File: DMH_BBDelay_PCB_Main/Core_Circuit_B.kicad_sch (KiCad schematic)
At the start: 68 parts, among them Q8 J113, SW1 SW_DPDT_x2, SW2 SW_DPDT_x2, SW4 SW_SPDT, U5 TL074, U6 TL074, U7 V3205, U8 CD4046, U9 40106

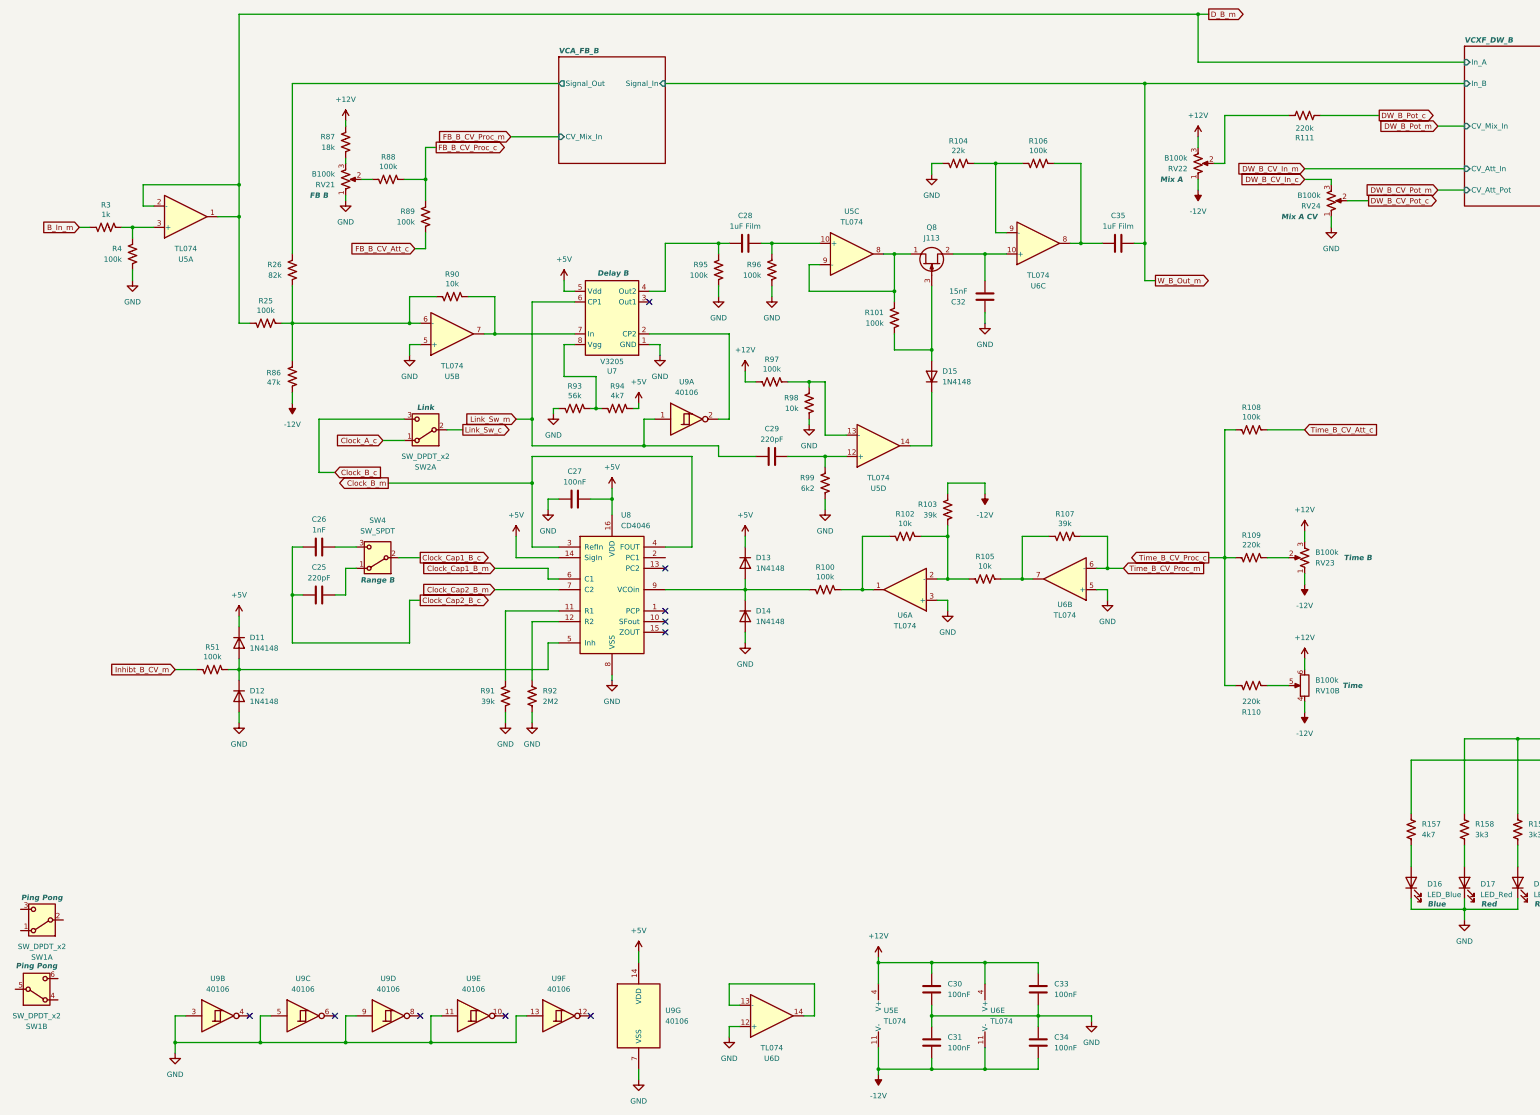
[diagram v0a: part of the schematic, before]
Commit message: Schematic in progress
Added AC coupling to inputs
Buffered wet outputs
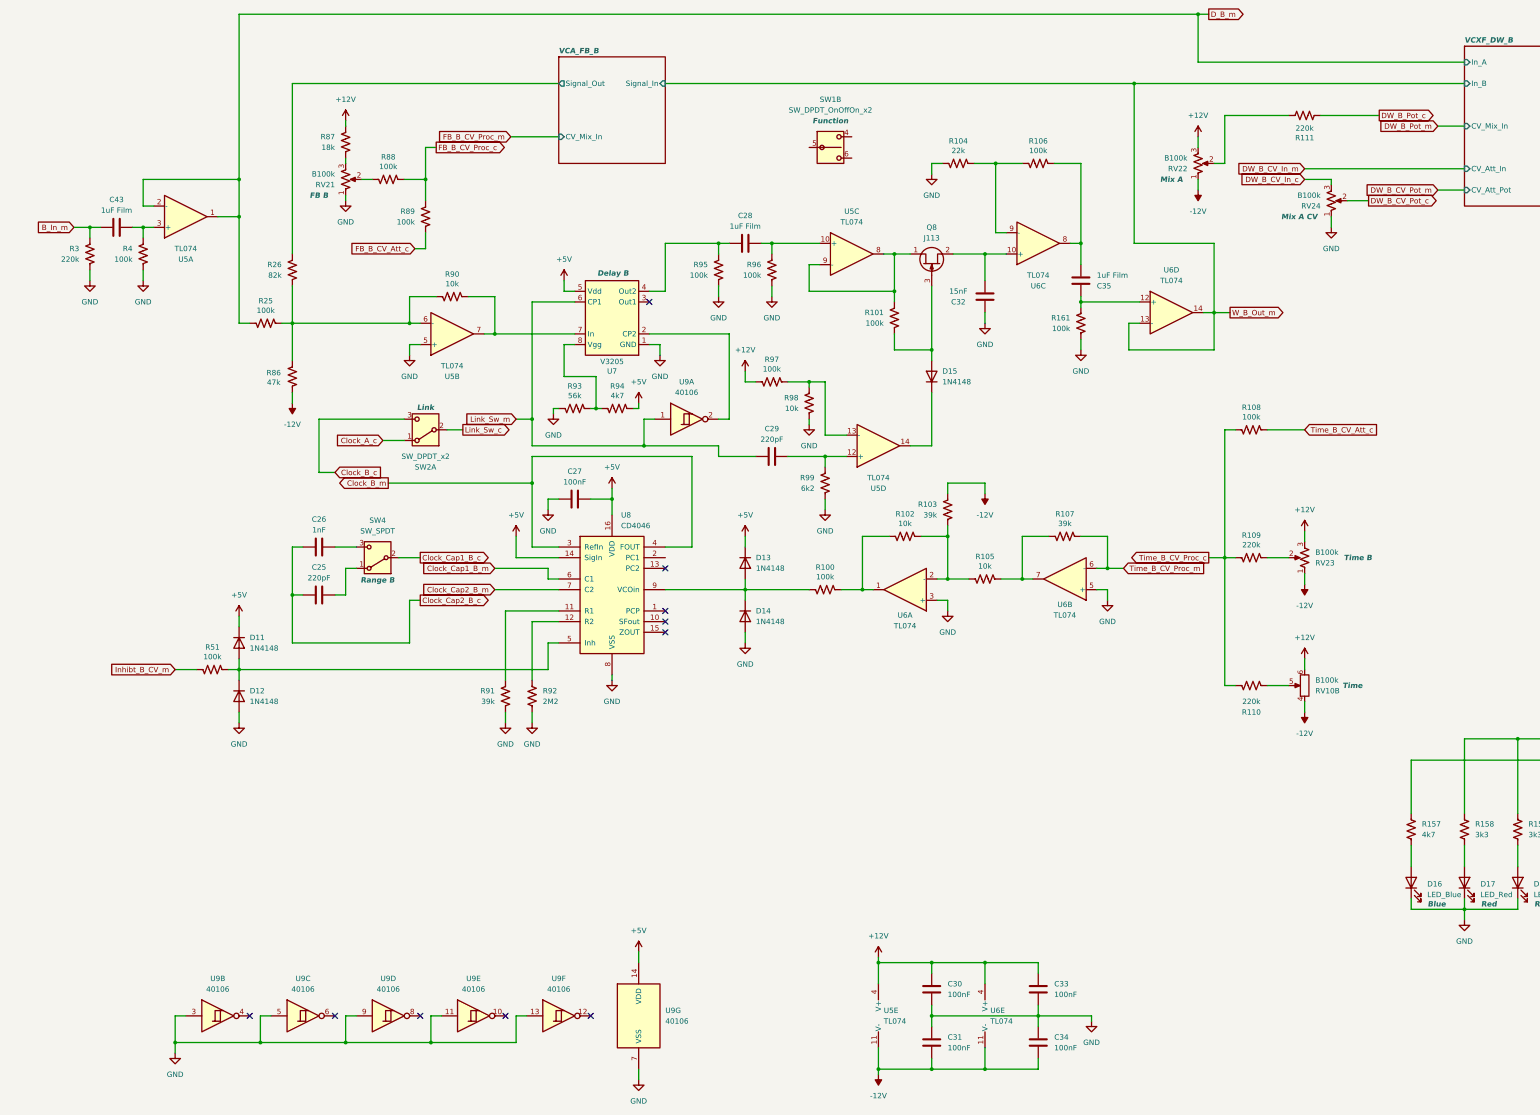
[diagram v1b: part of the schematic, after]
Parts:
- removed SW1: SW_DPDT_x2, symbol Switch:SW_DPDT_x2
- added C43: 1uF Film, Capacitor_THT:C_Disc_D7.5mm_W5.0mm_P5.00mm, symbol Device:C
- added R161: 100k, Resistor_THT:R_Axial_DIN0207_L6.3mm_D2.5mm_P7.62mm_Horizontal, symbol Device:R_US
- added SW1: SW_DPDT_OnOffOn_x2, SynthStuff:Toggle_Switch_2_Poles_TE, symbol SynthStuff:SW_DPDT_OnOffOn_x2
- C28, C35: footprint Capacitor_THT:C_Disc_D7.5mm_W4.4mm_P5.00mm -> Capacitor_THT:C_Disc_D7.5mm_W5.0mm_P5.00mm
- R3: value 1k -> 220k
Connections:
- net B_In_m: now also R3.2, C43.1; no longer R3.1
- net GND: now also R3.1, R161.1; no longer U6.12 (+)
- net W_B_Out_m: now also U6.13 (-), U6.14; no longer C35.2
- net at R4.2, U5.3 (+): now also C43.2; no longer R3.2
- net at R106.2, U6.8: now also C35.2; no longer C35.1
- new net: C35.1, R161.2, U6.12 (+)
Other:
- moved on the sheet: C35, R4, U6D

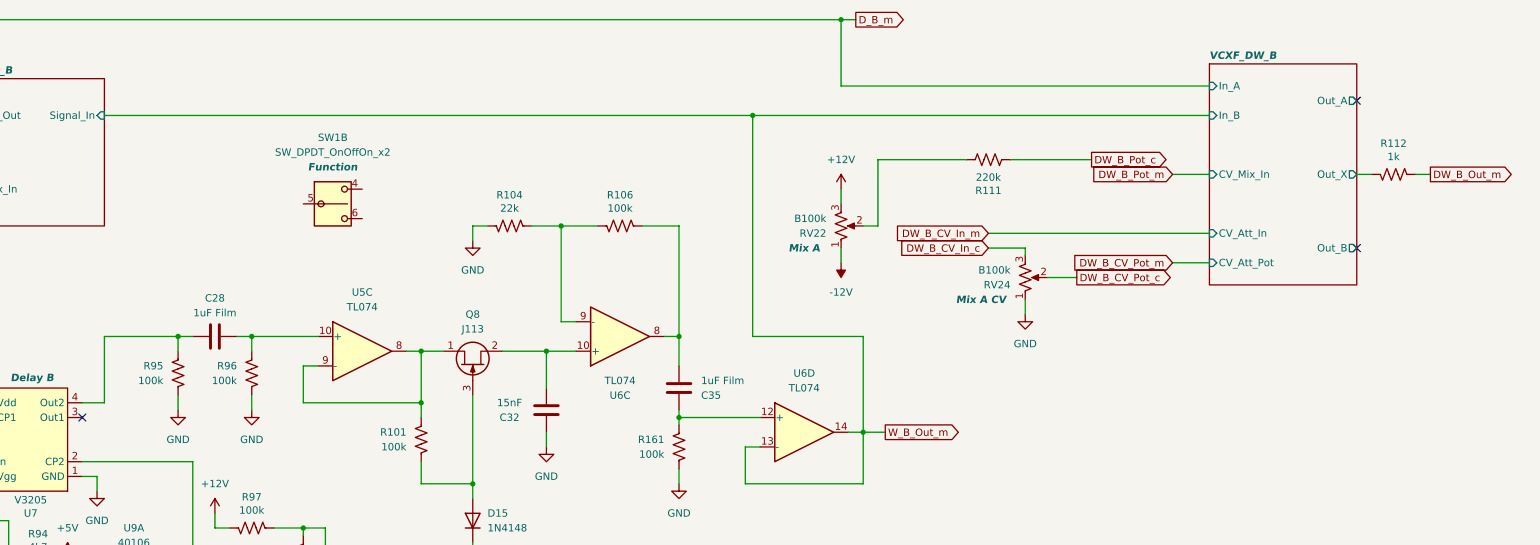
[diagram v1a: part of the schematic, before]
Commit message: Implemented Ping Pong funtion
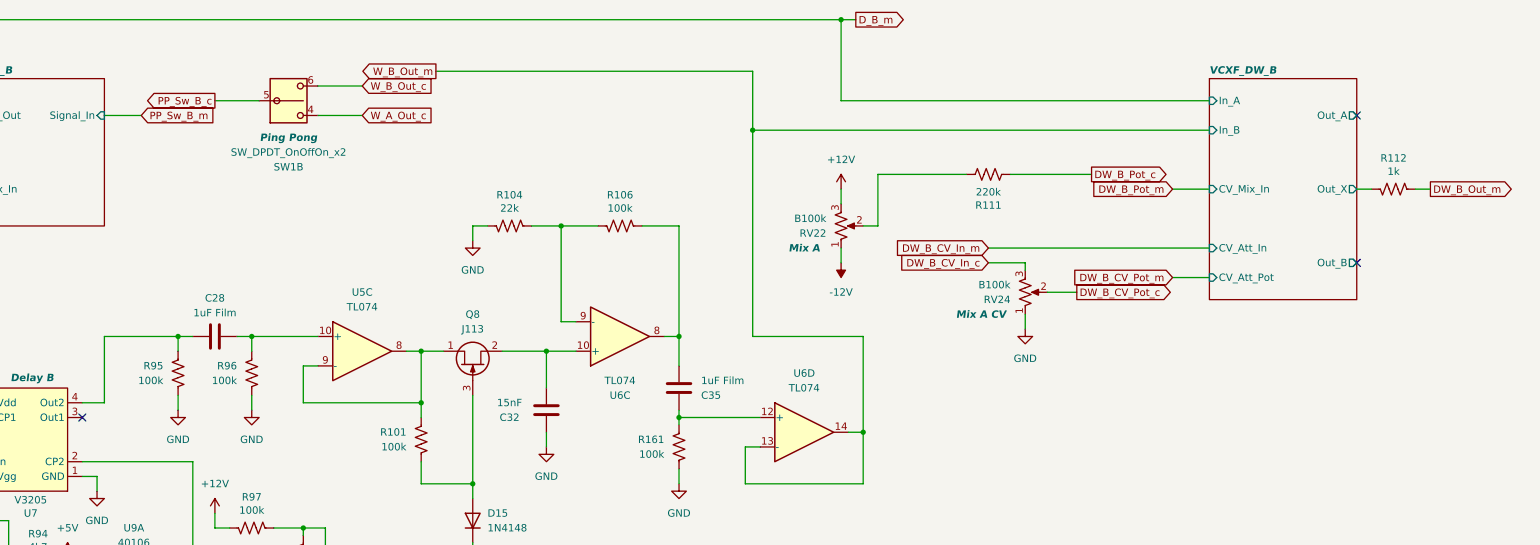
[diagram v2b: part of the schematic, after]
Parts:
- SW1: Function Function -> Ping Pong
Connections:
- net W_A_Out_c: now reaches SW1.4 (A)
- net PP_Sw_B_c: now reaches SW1.5 (B)
- net W_B_Out_c: now reaches SW1.6 (C)
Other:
- moved on the sheet: R111, R112, RV24, SW1B

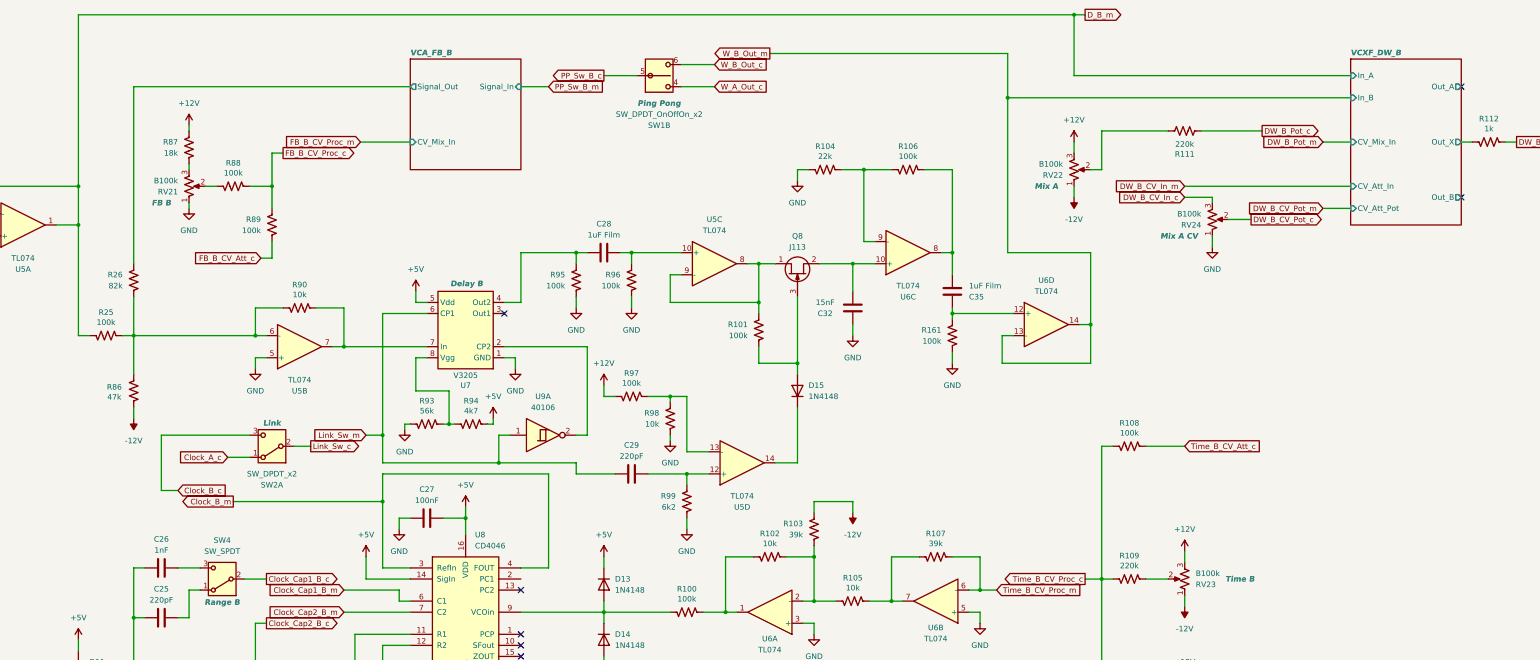
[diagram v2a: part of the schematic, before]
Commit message: Implemented tone control
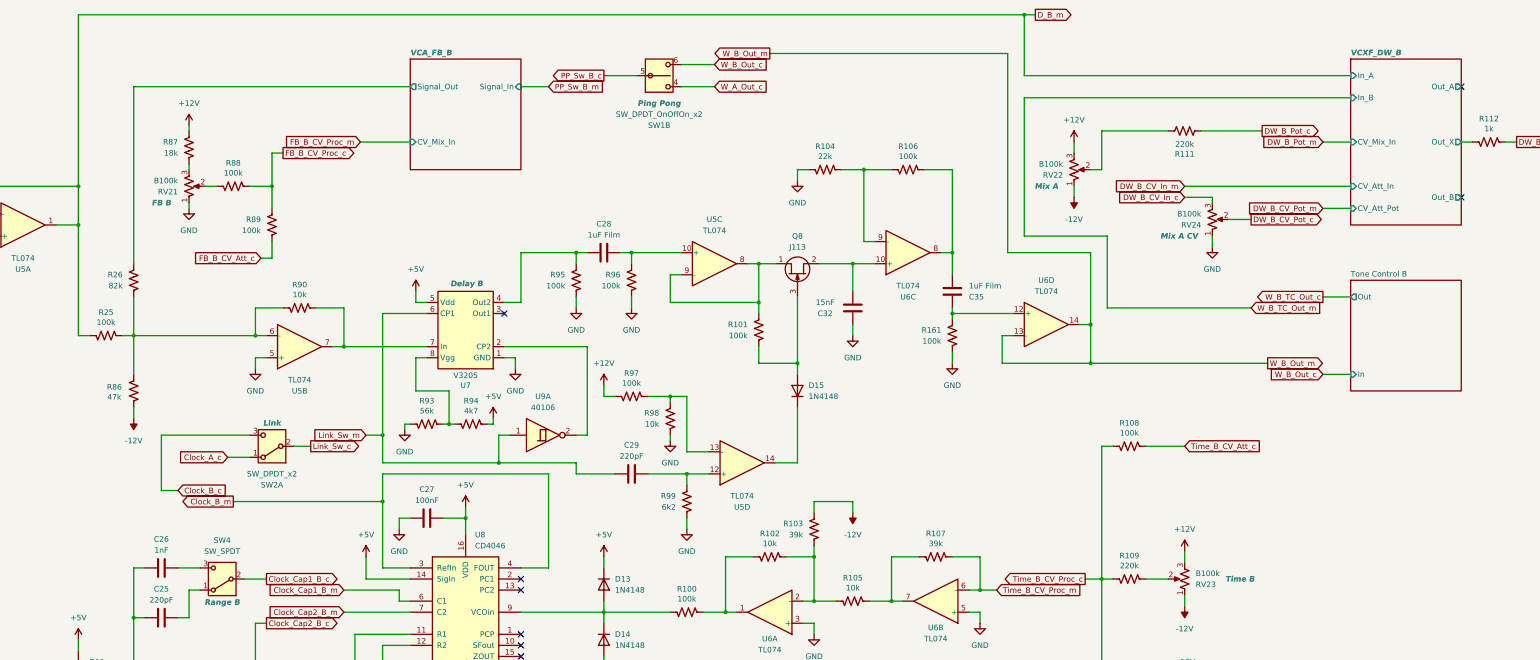
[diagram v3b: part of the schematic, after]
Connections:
- no-connect marks 12 -> 13
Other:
- added sheet Tone Control B (Tone_Control_B.kicad_sch)
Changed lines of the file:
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@@
 	)
 	(junction
+		(at 295.91 95.25)
+		(diameter 0)
+		(color 0 0 0 0)
+	)
+	(junction
 		(at 228.6 241.3)
 		(diameter 0)
@@
 	)
 	(junction
-		(at 292.1 15.24)
+		(at 280.67 15.24)
 		(diameter 0)
 		(color 0 0 0 0)
@@
 	)
 	(junction
-		(at 276.86 34.29)
-		(diameter 0)
-		(color 0 0 0 0)
-	)
-	(junction
 		(at 219.71 72.39)
 		(diameter 0)
@@
 	)
 	(no_connect
+		(at 165.1 144.78)
+	)
+	(no_connect
 		(at 381 31.75)
 	)
@@
 	(wire
 		(pts
-			(xy 355.6 29.21) (xy 292.1 29.21)
+			(xy 355.6 29.21) (xy 280.67 29.21)
 		)
 		(stroke
@@
 	(wire
 		(pts
-			(xy 276.86 34.29) (xy 276.86 69.85)
+			(xy 276.86 24.13) (xy 276.86 69.85)
 		)
 		(stroke
@@
 	(wire
 		(pts
+			(xy 299.72 82.55) (xy 299.72 66.04)
+		)
+		(stroke
+			(width 0)
+			(type default)
+		)
+	)
+	(wire
+		(pts
 			(xy 212.09 152.4) (xy 214.63 152.4)
 		)
@@
 	(wire
 		(pts
+			(xy 295.91 95.25) (xy 336.55 95.25)
+		)
+		(stroke
+			(width 0)
+			(type default)
+		)
+	)
+	(wire
+		(pts
 			(xy 228.6 80.01) (xy 228.6 95.25)
 		)
@@
 	(wire
 		(pts
+			(xy 299.72 82.55) (xy 332.74 82.55)
+		)
+		(stroke
+			(width 0)
+			(type default)
+		)
+	)
+	(wire
+		(pts
+			(xy 349.25 80.01) (xy 355.6 80.01)
+		)
+		(stroke
+			(width 0)
+			(type default)
+		)
+	)
+	(wire
+		(pts
 			(xy 106.68 93.98) (xy 104.14 93.98)
 		)
@@
 	(wire
 		(pts
-			(xy 292.1 29.21) (xy 292.1 15.24)
+			(xy 280.67 29.21) (xy 280.67 15.24)
 		)
 		(stroke
@@
 	(wire
 		(pts
-			(xy 276.86 34.29) (xy 355.6 34.29)
-		)
-		(stroke
-			(width 0)
-			(type default)
-		)
-	)
-	(wire
-		(pts
 			(xy 355.6 226.06) (xy 355.6 228.6)
 		)
@@
 	(wire
 		(pts
+			(xy 280.67 66.04) (xy 280.67 34.29)
+		)
+		(stroke
+			(width 0)
+			(type default)
+		)
+	)
+	(wire
+		(pts
 			(xy 92.71 54.61) (xy 95.25 54.61)
 		)
@@
 	(wire
 		(pts
-			(xy 292.1 15.24) (xy 294.64 15.24)
+			(xy 280.67 15.24) (xy 283.21 15.24)
 		)
 		(stroke
@@
 	(wire
 		(pts
+			(xy 299.72 66.04) (xy 280.67 66.04)
+		)
+		(stroke
+			(width 0)
+			(type default)
+		)
+	)
+	(wire
+		(pts
 			(xy 88.9 260.35) (xy 68.58 260.35)
 		)
@@
 	(wire
 		(pts
-			(xy 226.06 139.7) (xy 232.41 139.7)
+			(xy 349.25 97.79) (xy 355.6 97.79)
 		)
 		(stroke
@@
 	(wire
 		(pts
-			(xy 129.54 254) (xy 129.54 260.35)
+			(xy 226.06 139.7) (xy 232.41 139.7)
 		)
 		(stroke
@@
 	(wire
 		(pts
-			(xy 308.61 175.26) (xy 313.69 175.26)
+			(xy 129.54 254) (xy 129.54 260.35)
 		)
 		(stroke
@@
 	(wire
 		(pts
-			(xy 276.86 24.13) (xy 276.86 34.29)
+			(xy 308.61 175.26) (xy 313.69 175.26)
 		)
 		(stroke
@@
 	(wire
 		(pts
+			(xy 280.67 34.29) (xy 355.6 34.29)
+		)
+		(stroke
+			(width 0)
+			(type default)
+		)
+	)
+	(wire
+		(pts
 			(xy 355.6 228.6) (xy 368.3 228.6)
 		)
@@
 	(wire
 		(pts
-			(xy 292.1 15.24) (xy 63.5 15.24)
+			(xy 280.67 15.24) (xy 63.5 15.24)
 		)
 		(stroke
@@
 	(global_label "D_B_m"
 		(shape output)
-		(at 294.64 15.24 0)
+		(at 283.21 15.24 0)
 		(fields_autoplaced yes)
 		(effects
@@
 		)
 		(property "Intersheetrefs" "${INTERSHEET_REFS}"
-			(at 303.7937 15.24 0)
+			(at 292.3637 15.24 0)
 			(hide yes)
 			(show_name no)
@@
 		)
 	)
+	(global_label "W_B_TC_Out_m"
+		(shape input)
+		(at 332.74 82.55 0)
+		(fields_autoplaced yes)
+		(effects
+			(font
+				(size 1.27 1.27)
+			)
+			(justify left)
+		)
+		(property "Intersheetrefs" "${INTERSHEET_REFS}"
+			(at 349.4531 82.55 0)
+			(hide yes)
+			(show_name no)
+			(do_not_autoplace no)
+			(effects
+				(font
+					(size 1.27 1.27)
+				)
+				(justify left)
+			)
+		)
+	)
+	(global_label "W_B_Out_c"
+		(shape input)
+		(at 349.25 97.79 180)
+		(fields_autoplaced yes)
+		(effects
+			(font
+				(size 1.27 1.27)
+			)
+			(justify right)
+		)
+		(property "Intersheetrefs" "${INTERSHEET_REFS}"
+			(at 336.3468 97.79 0)
+			(hide yes)
+			(show_name no)
+			(do_not_autoplace no)
+			(effects
+				(font
+					(size 1.27 1.27)
+				)
+				(justify right)
+			)
+		)
+	)
 	(global_label "PP_Sw_B_m"
 		(shape input)
@@
 		)
 	)
+	(global_label "W_B_TC_Out_c"
+		(shape output)
+		(at 349.25 80.01 180)
+		(fields_autoplaced yes)
+		(effects
+			(font
+				(size 1.27 1.27)
+			)
+			(justify right)
+		)
+		(property "Intersheetrefs" "${INTERSHEET_REFS}"
+			(at 333.1416 80.01 0)
+			(hide yes)
+			(show_name no)
+			(do_not_autoplace no)
+			(effects
+				(font
+					(size 1.27 1.27)
+				)
+				(justify right)
+			)
+		)
+	)
 	(global_label "Inhibt_B_CV_m"
 		(shape input)
@@
 		)
 	)
+	(global_label "W_B_Out_m"
+		(shape output)
+		(at 336.55 95.25 0)
+		(fields_autoplaced yes)
+		(effects
+			(font
+				(size 1.27 1.27)
+			)
+			(justify left)
+		)
+		(property "Intersheetrefs" "${INTERSHEET_REFS}"
+			(at 350.0579 95.25 0)
+			(hide yes)
+			(show_name no)
+			(do_not_autoplace no)
+			(effects
+				(font
+					(size 1.27 1.27)
+				)
+				(justify left)
+			)
+		)
+	)
 	(global_label "Link_Sw_c"
 		(shape output)
@@
 	)
 	(sheet
+		(at 355.6 76.2)
+		(size 25.4 25.4)
+		(exclude_from_sim no)
+		(in_bom yes)
+		(on_board yes)
+		(dnp no)
+		(fields_autoplaced yes)
+		(stroke
+			(width 0.1524)
+			(type solid)
+		)
+		(fill
+			(color 0 0 0 0)
+		)
+		(property "Sheetname" "Tone Control B"
+			(at 355.6 75.4884 0)
+			(show_name no)
+			(do_not_autoplace no)
+			(effects
+				(font
+					(size 1.27 1.27)
+				)
+				(justify left bottom)
+			)
+		)
+		(property "Sheetfile" "Tone_Control_B.kicad_sch"
+			(at 355.6 102.1846 0)
+			(hide yes)
+			(show_name no)
+			(do_not_autoplace no)
+			(effects
+				(font
+					(size 1.27 1.27)
+				)
+				(justify left top)
+			)
+		)
+		(pin "In" input
+			(at 355.6 97.79 180)
+			(effects
+				(font
+					(size 1.27 1.27)
+				)
+				(justify left)
+			)
+		)
+		(pin "Out" output
+			(at 355.6 80.01 180)
+			(effects
+				(font
+					(size 1.27 1.27)
+				)
+				(justify left)
+			)
+		)
+		(instances
+			(project "DMH_BBDelay_PCB_Main"
+				(path "/58f4306d-5387-4983-bb08-41a2313fd315/53120047-129a-4e0f-876f-6cafa2f18733"
+					(page "11")
+				)
+			)
+		)
+	)
+	(sheet
 		(at 355.6 25.4)
 		(size 25.4 38.1)
@@
 			(project "DMH_BBDelay_PCB_Main"
 				(path "/58f4306d-5387-4983-bb08-41a2313fd315/53120047-129a-4e0f-876f-6cafa2f18733"
-					(page "10")
+					(page "9")
 				)
 			)
@@
 			(project "DMH_BBDelay_PCB_Main"
 				(path "/58f4306d-5387-4983-bb08-41a2313fd315/53120047-129a-4e0f-876f-6cafa2f18733"
-					(page "9")
+					(page "8")
 				)
 			)
